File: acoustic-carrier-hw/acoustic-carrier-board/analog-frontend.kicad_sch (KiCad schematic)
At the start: 90 parts, among them IC1 ECP5-BGA256, J1 BWU.FL-IPEX1, J10 BWU.FL-IPEX1, J11 BWU.FL-IPEX1, J17 BWU.FL-IPEX1, J2 Conn_02x08_Odd_Even, J22 8P8C_Shielded, J4 BWU.FL-IPEX1, J5 BWU.FL-IPEX1, J7 BWU.FL-IPEX1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

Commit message: [carrier] Added hierarchical labels
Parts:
- removed IC1: ECP5-BGA256, iw-fpga_mcu:BGA256C80P16X16_1400X1400X170, symbol iw-fpga_mcu:ECP5-BGA256
- removed J2: Conn_02x08_Odd_Even, Connector_PinSocket_2.54mm:PinSocket_2x08_P2.54mm_Horizontal, symbol Connector_Generic:Conn_02x08_Odd_Even
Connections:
- net ADC_IN12_SW is gone; now on net FPGA_ADC_SW: U2.14 (IN1-2)
- net FPGA_LED0 is gone; now on net FPGA_ADC_LED0: R128.2, R129.2
- net FPGA_LED1 is gone; now on net FPGA_ADC_LED1: R126.2, R127.1
- no-connect marks 9 -> 8
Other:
- note removed: "FPGA BANK"
- note removed: "SIGNAL CONNECTOR"

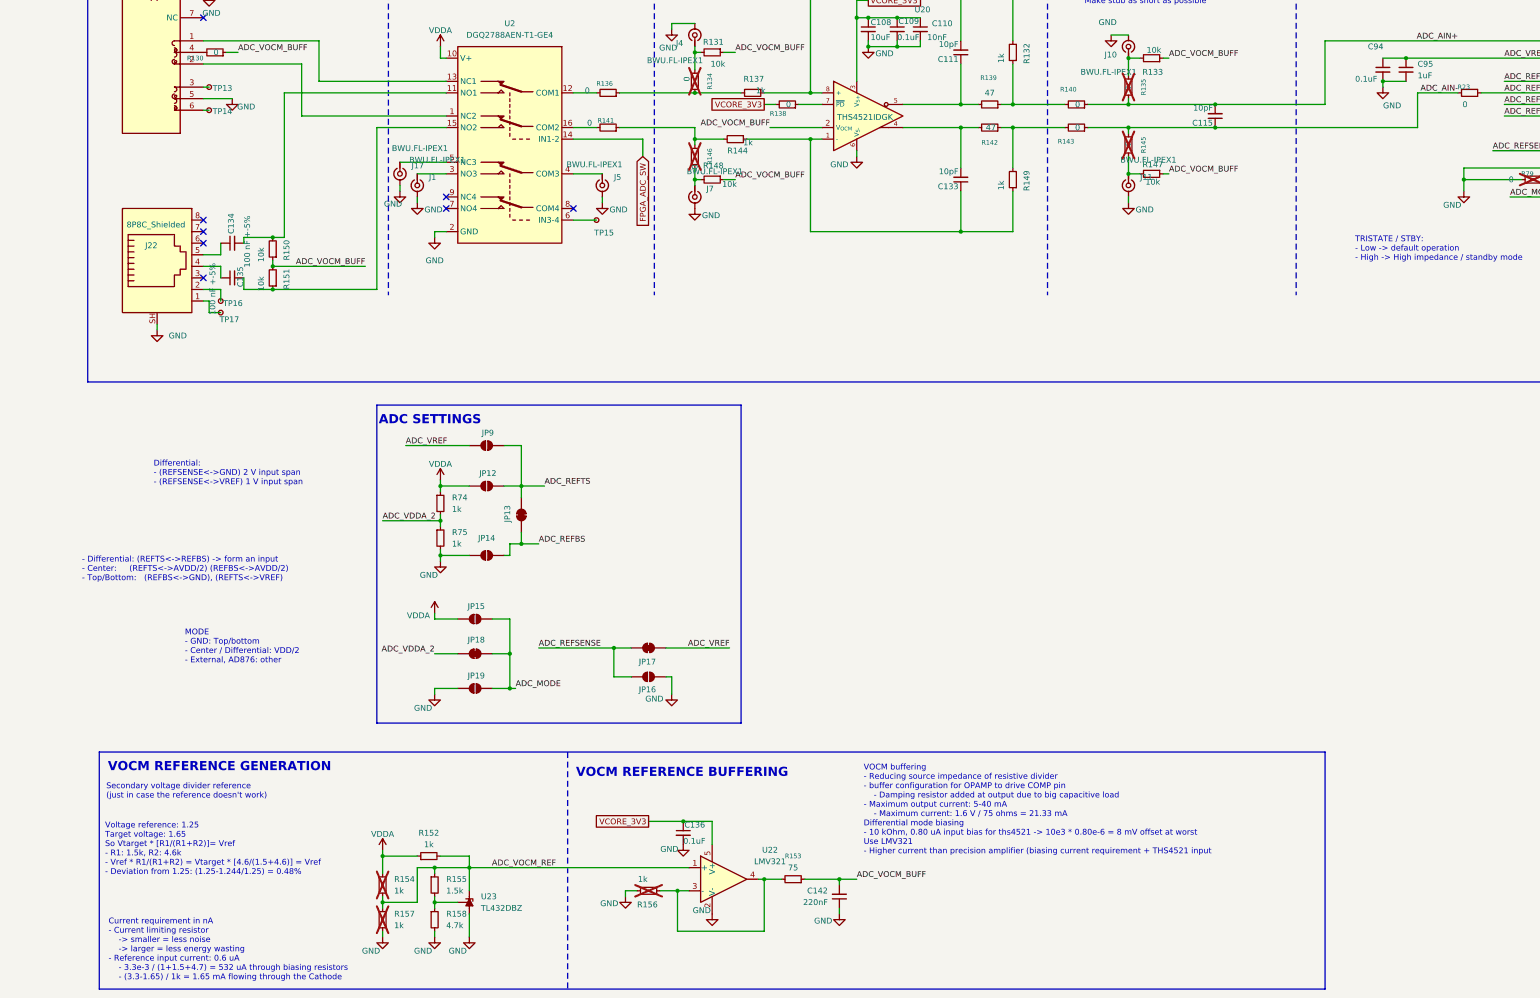
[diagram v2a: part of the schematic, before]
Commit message: [¢arrier] Did major cchecks of ETH, DDR, ANALOG, config (next) check buffer circuit driven by USB-CC, then start layout
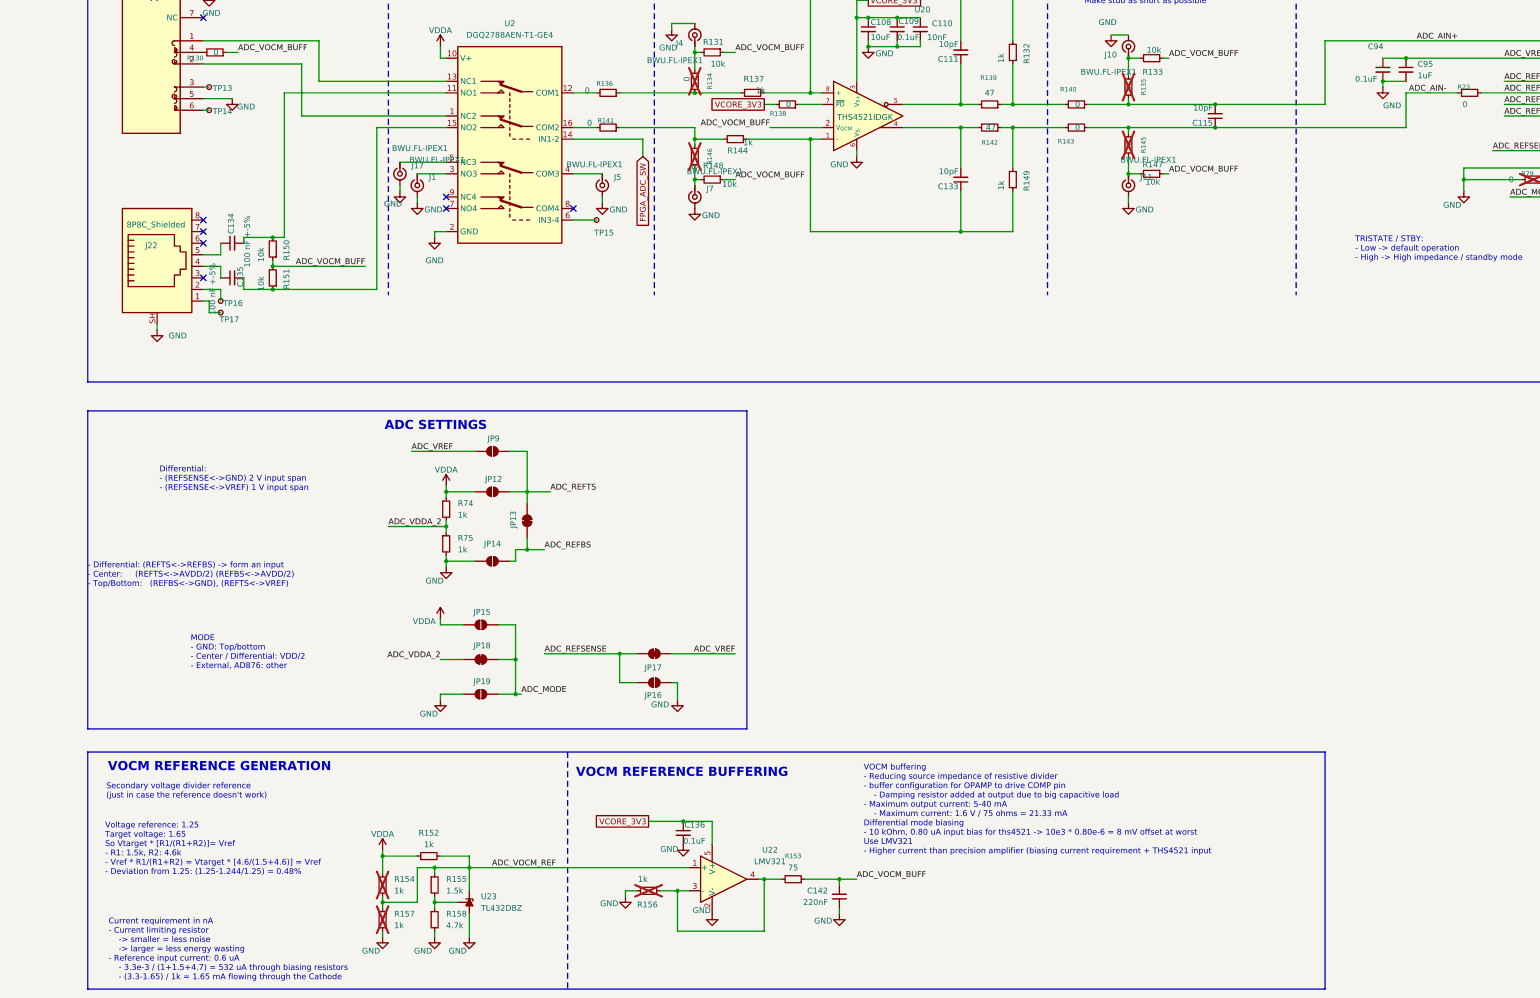
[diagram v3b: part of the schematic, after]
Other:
- moved on the sheet: JP12, JP13, JP14, JP15, JP16, JP17, JP18, JP19, JP9, R74, R75

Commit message: [carrier] Did some check for example schematics, starting layout
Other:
- moved on the sheet: J4, J7, R131, R134, R146, R148

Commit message: [carrier] Added testpoints
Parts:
- removed TP13, TP14, TP15, TP16, TP17: TestPoint_Small, TestPoint:TestPoint_Pad_D1.5mm, symbol Connector:TestPoint_Small
- added TP13, TP14, TP16, TP2, TP26, TP27, TP28, TP29, TP30, TP31, TP32: TestPoint, TestPoint:TestPoint_Loop_D1.80mm_Drill1.0mm_Beaded, symbol Connector:TestPoint
- added TP17: TestPoint, TestPoint:TestPoint_Pad_1.0x1.0mm, symbol Connector:TestPoint
- C110: LPN CL05B103KB5NNNC -> C15195; MPN C15195 -> CL05B103KB5NNNC
- C111, C115, C133: footprint Capacitor_SMD:C_0603_1608Metric -> Capacitor_SMD:C_0603_1608Metric_Pad1.08x0.95mm_HandSolder
- R132, R137, R144, R149, R152, R74, R75: LPN 0603WAF1001T5E -> C21190; MPN C21190 -> 0603WAF1001T5E
- R155: value 1.5k -> 1k5; LPN 0603WAF1501T5E -> C22843; MPN C22843 -> 0603WAF1501T5E
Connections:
- net ADC_MODE: now also TP30.1
- net ADC_REFBS: now also TP28.1
- net ADC_REFSENSE: now also TP29.1
- net ADC_VOCM_BUFF: now also TP26.1
- net ADC_VOCM_REF: now also TP27.1
- net FPGA_ADC_SW: now also TP32.1
- net VDDA: now also TP31.1
- net at RJ1.3: now also TP2.1
- net RJ45_ADC_AIN+: now reaches C134.2, R150.2, U2.11 (NO1)
- net MAG_ADC_AIN+: now reaches RJ1.1, U2.13 (NC1)
- net MAG_ADC_AIN-: now reaches RJ1.2, U2.1 (NC2)
- net at RJ1.6: now also TP14.1
- net RJ45_ADC_AIN-: now reaches C135.2, R151.1, U2.15 (NO2)
- net at U2.6 (IN3-4): now also TP17.1
- net at J22.2: now also TP16.1
- net at J22.1: now also TP13.1
- net CLK renamed ADC.CLK
- net D0 renamed ADC.D0
- net D1 renamed ADC.D1
- net D2 renamed ADC.D2
- net D3 renamed ADC.D3
- net D4 renamed ADC.D4
- net D5 renamed ADC.D5
- net D6 renamed ADC.D6
- net D7 renamed ADC.D7
- net D8 renamed ADC.D8
- net D9 renamed ADC.D9
- net OTR renamed ADC.OTR
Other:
- moved on the sheet: C93, R136, R141, R23
